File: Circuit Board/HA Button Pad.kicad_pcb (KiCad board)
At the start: 2 copper layers, 119.4 x 72.4 mm, 54 parts, among them P1 USB C Connector, Q1 PN2222A, SW1 Button 1, SW2 Button 2, SW3 Button 3, SW4 Button 4, SW5 Bank Up, SW6 Bank Down, SW7 Program Button, U1 WT32-ETH01, U3 CP2102N, U4 Char LCD I2C, U5 Button I2C

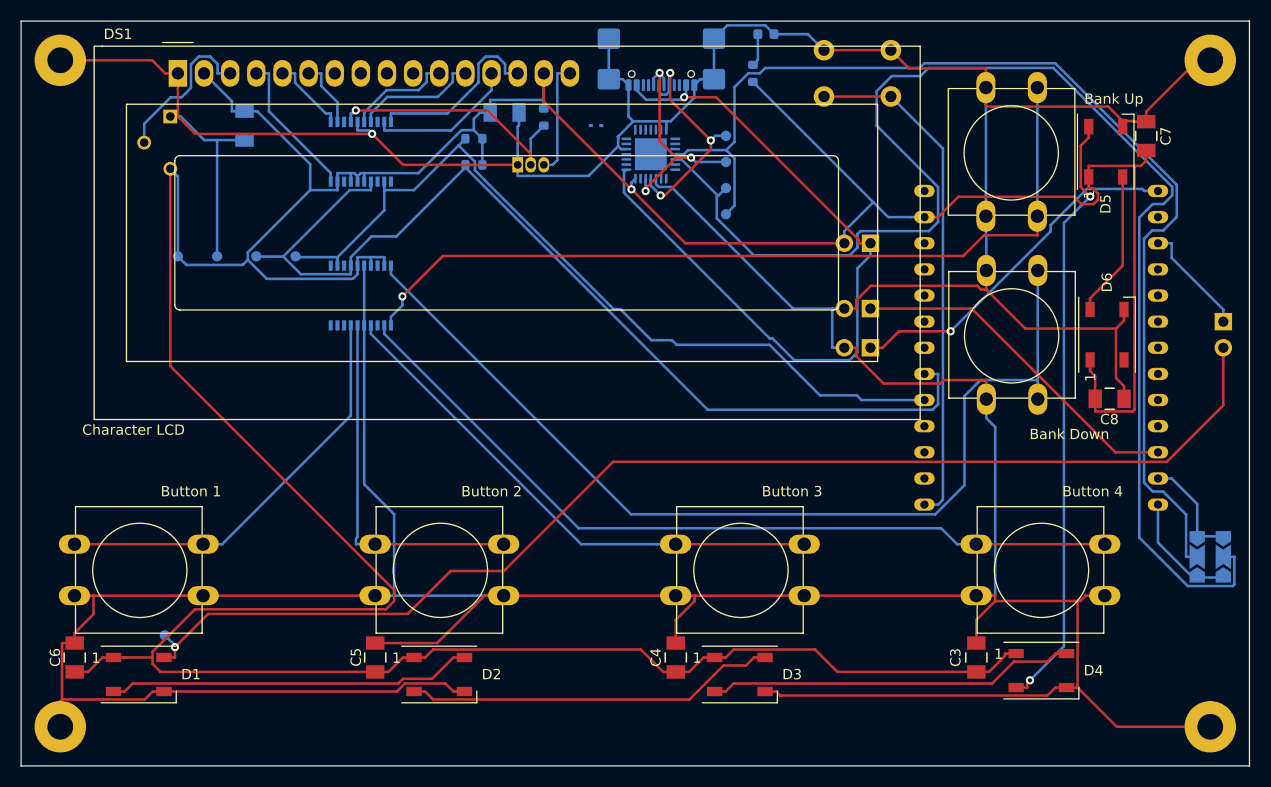
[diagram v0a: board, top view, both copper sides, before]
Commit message: Added Capacitive Touch, changed ESP32 Pin Assignment
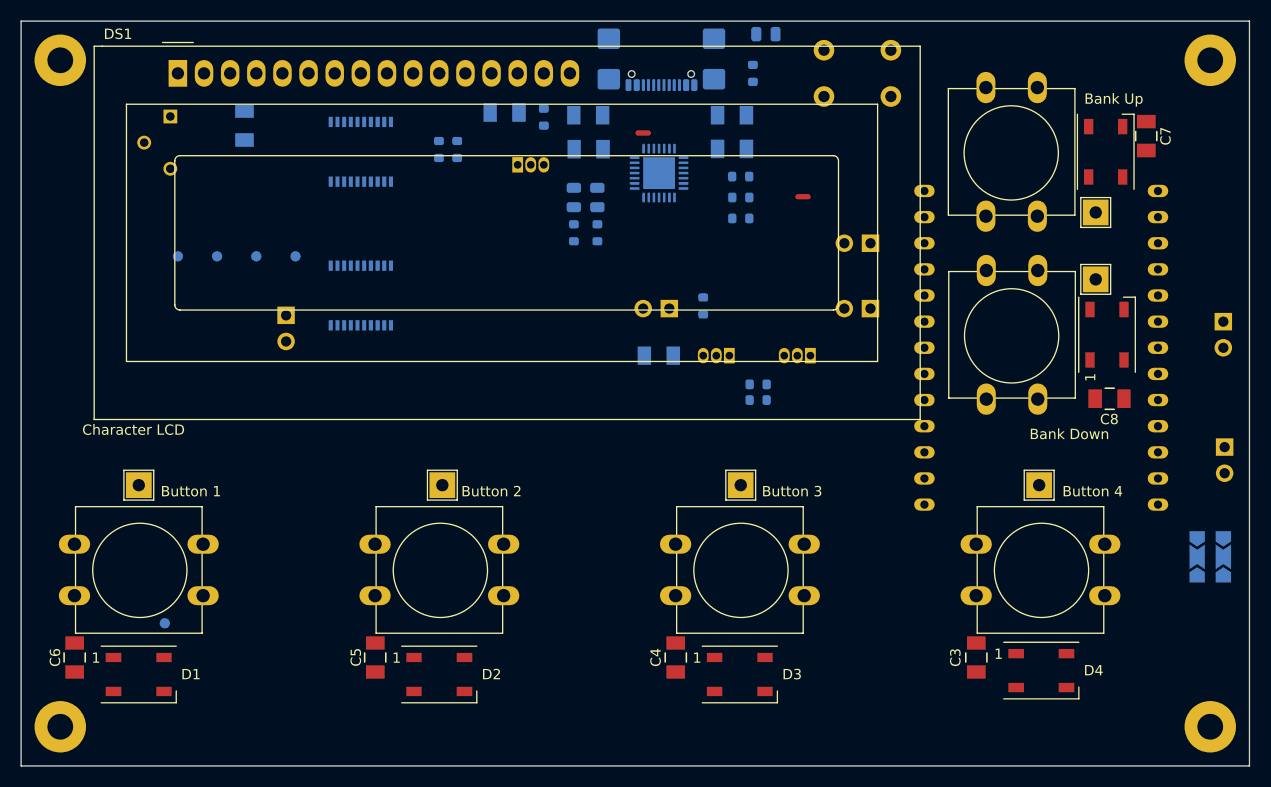
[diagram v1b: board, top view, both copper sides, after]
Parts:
- removed D8: D_Zener, tvs diode D5:SOD923_DIO
- removed TP1: USB D+, TestPoint:TestPoint_Pad_D1.0mm
- removed TP2: USB D-, TestPoint:TestPoint_Pad_D1.0mm
- removed TP3: CP2102 TXD, TestPoint:TestPoint_Pad_D1.0mm
- removed TP4: CP2102 RXD, TestPoint:TestPoint_Pad_D1.0mm
- added C10: 0.1uF, capacitor model:CAPC340180_88N_KEM, B.Cu at (104.6, 34.5)
- added C11: 4.7uF, capacitor model:CAPC340180_88N_KEM, B.Cu at (90.7, 34.5)
- added C12: 0.1uF, capacitor model:CAPC340180_88N_KEM, B.Cu at (90.7, 37.8)
- added C13: 1uF, capacitor model:CAPC340180_88N_KEM, B.Cu at (97.5, 57.9)
- added C9: 4.7uF, capacitor model:CAPC340180_88N_KEM, B.Cu at (104.6, 37.8)
- added D10: RX LED, LED_SMD:LED_0805_2012Metric, B.Cu at (91.6, 42.5)
- added D9: TX LED, LED_SMD:LED_0805_2012Metric, B.Cu at (89.3, 42.5)
- added J2: RX and TX, Connector_PinHeader_2.54mm:PinHeader_1x02_P2.54mm_Vertical, B.Cu at (152.5, 66.8)
- added J3: GND and VCC, Connector_PinHeader_2.54mm:PinHeader_1x02_P2.54mm_Vertical, B.Cu at (61.3, 54.0)
- added NT1: NetTie_2, NetTie:NetTie-2_SMD_Pad0.5mm, F.Cu at (111.5, 42.5)
- added NT2: NetTie_2, NetTie:NetTie-2_SMD_Pad0.5mm, F.Cu at (96.0, 36.3)
- added Q2: 2N2222A, Package_TO_SOT_THT:TO-92_Inline, B.Cu at (104.4, 57.9)
- added Q3: 2N2222A, Package_TO_SOT_THT:TO-92_Inline, B.Cu at (112.3, 57.9)
- added R10: 10K, Resistor_SMD:R_0603_1608Metric, B.Cu at (101.9, 53.1)
- added R11: 22.1K, Resistor_SMD:R_0603_1608Metric, B.Cu at (105.5, 42.5)
- added R12: 47.5K, Resistor_SMD:R_0603_1608Metric, B.Cu at (105.5, 44.6)
- added R5: CP2102 Reset Pullup, Resistor_SMD:R_0603_1608Metric, B.Cu at (105.5, 40.5)
- added R6: TX LED Resistor, Resistor_SMD:R_0603_1608Metric, B.Cu at (89.3, 46.0)
- added R7: RX LED Resistor, Resistor_SMD:R_0603_1608Metric, B.Cu at (91.6, 46.0)
- added R8: 10K, Resistor_SMD:R_0603_1608Metric, B.Cu at (107.2, 62.2)
- added R9: 10K, Resistor_SMD:R_0603_1608Metric, B.Cu at (107.2, 60.7)
- added TP12: Button 3 Touch, TestPoint:TestPoint_THTPad_2.5x2.5mm_Drill1.2mm, F.Cu at (105.5, 70.5)
- added TP13: Button 4 Touch, TestPoint:TestPoint_THTPad_2.5x2.5mm_Drill1.2mm, F.Cu at (134.5, 70.5)
- added TP14: Button Up Touch, TestPoint:TestPoint_THTPad_2.5x2.5mm_Drill1.2mm, F.Cu at (140.0, 44.0)
- added TP15: Button Down Touch, TestPoint:TestPoint_THTPad_2.5x2.5mm_Drill1.2mm, F.Cu at (140.0, 50.5)
- added TP5: Button 1 Touch, TestPoint:TestPoint_THTPad_2.5x2.5mm_Drill1.2mm, F.Cu at (47.0, 70.5)
- added TP6: Button 2 Touch, TestPoint:TestPoint_THTPad_2.5x2.5mm_Drill1.2mm, F.Cu at (76.5, 70.5)
- D7: footprint LED_SMD:LED_0603_1608Metric -> LED_SMD:LED_0805_2012Metric
- JP1: value Programming Jumper -> Upload
- JP2: value USB Power Jumper -> USB Power
- JP3: value Run Program Jumper -> Run Prgm
- JP5: value CP2102 RX -> CP2102N RX
- JP6: value CP2102 TX -> CP2102N TX
- Q1: value PN2222A -> 2N2222A
- moved JP3 19.9 mm to (98.6, 53.3)
- moved R3 3.55 mm to (76.2, 37.9), turned to 90 degrees
- moved R2 2.20 mm to (77.9, 37.9), turned to 90 degrees
- moved U3 2.00 mm to (97.6, 40.2), turned to -90 degrees
- moved TP11 1.17 mm to (49.5, 83.9)
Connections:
- U1 pad 15: unconnected-(U1-IO2/ADC2_CH2/TCH2/PRG_FLOAT_OR_GND-Pad15) -> Button 3 Touch
- U1 pad 16: Net-(JP4-A) -> Button 1 Touch
- U1 pad 18: unconnected-(U1-IO12/ADC2_CH5/TCH5/BOOT_FLOAT_OR_LOW-Pad18) -> Button 4 Touch
- U1 pad 19: unconnected-(U1-IO14/ADC2_CH6/TCH6-Pad19) -> SDA
- U1 pad 20: unconnected-(U1-IO15/ADC2_CH3/TCH3-Pad20) -> Button 2 Touch
- U1 pad 5: SCL -> Button Down Touch
- U1 pad 6: SDA -> Button Up Touch
- U1 pad 7: unconnected-(U1-IO5/BOOT_FLOAT-Pad7) -> SCL
- U1 pad 8: unconnected-(U1-IO17/UART2_TX-Pad8) -> WS2812b LED Data
- U3 pad 12: GND -> Net-(C10-Pad2)
- U3 pad 18: unconnected-(U3-~{RXT}/GPIO.1-Pad18) -> Net-(D10-K)
- U3 pad 19: unconnected-(U3-~{TXT}/GPIO.0-Pad19) -> Net-(D9-K)
- U3 pad 21: GND -> Net-(C10-Pad2)
- U3 pad 23: unconnected-(U3-~{CTS}-Pad23) -> (no net)
- U3 pad 24: unconnected-(U3-~{RTS}-Pad24) -> RTS
- U3 pad 28: (no net) -> DTR
- U3 pad 29: (no net) -> Net-(C10-Pad2)
- U3 pad 3: GND -> Net-(C10-Pad2)
- U3 pad 6: unconnected-(U3-VDD-Pad6) -> Net-(U3-VDD)
- U3 pad 7: VBUS -> Net-(U3-VREGIN)
- U3 pad 8: Net-(JP2-A) -> Net-(U3-VBUS)
- U3 pad 9: unconnected-(U3-~{RST}-Pad9) -> Net-(U3-~{RST})
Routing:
- net GND: track 571.7 -> 0.00 mm, vias 1 -> 0
- net VBUS: track 400.6 -> 0.00 mm, vias 1 -> 0
- net Net-(JP6-C): track 134.7 -> 0.00 mm
- net WS2812b LED Data: track 120.9 -> 0.00 mm, vias 1 -> 0
- net Net-(JP5-C): track 108.8 -> 0.00 mm
- net SDA: track 98.8 -> 0.00 mm
- net Bank Down Button: track 96.3 -> 0.00 mm
- net Bank Up Button: track 81.8 -> 0.00 mm, vias 1 -> 0
- net SCL: track 80.1 -> 0.00 mm
- net Button 4: track 79.3 -> 0.00 mm
- net Net-(JP2-A): track 74.3 -> 0.00 mm, vias 1 -> 0
- net Net-(D4-DOUT): track 58.8 -> 0.00 mm, vias 2 -> 0
- net Button 3: track 51.4 -> 0.00 mm
- net Net-(Q2-C): track 49.8 -> 0.00 mm
- net Button 1: track 40.8 -> 0.00 mm
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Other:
- board text added: "+"
- board text added: "-"
- board text added: "0.1uF"
- board text added: "1"
- board text added: "10K"
- board text added: "1K"
- board text added: "1uF"
- board text added: "28"
- board text added: "4.7uF"
- board text added: "5v"
- board text added: "GND"
- board text added: "Home Assistant Button Panel v1.3 https://github.com/PKCubed/HAButtonPad"
- board text added: "RX"
- board text added: "TX"
- board text removed: "Home Assistant Button Panel v1.1 https://github.com/PKCubed/HAButtonPad"
